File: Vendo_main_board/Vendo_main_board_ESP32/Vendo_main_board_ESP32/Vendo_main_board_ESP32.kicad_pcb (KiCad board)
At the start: 2 copper layers, 60 x 100 mm, 125 parts, among them J1 Screw_Terminal_01x04, J10 Screw_Terminal_01x03, J11 Screw_Terminal_01x02, J12 Screw_Terminal_01x03, J2 Barrel_Jack_MountingPin, J3 Conn_01x05_Pin, J4 Conn_01x05_Pin, J6 Screw_Terminal_01x04, J7 FTDI, J9 Conn_01x04_Pin, Q1 Q_NMOS_Depletion_GSD, Q2 Q_NMOS_Depletion_GSD, Q3 Q_NMOS_Depletion_GSD, Q4 Q_NMOS_Depletion_GSD, SW1 SW_Push, SW2 SW_Push, SW3 SW_Push, SW5 SW_Slide_DPDT, SW7 SW_Push, U1 AMS1117-3.3, U2 TPS54331D, U4 PC817, U5 TPL5010, U6 SOLA-IC SLM1302, U7 ESP32-WROOM-32, Y1 Crystal

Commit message: -esp 32 version done routing
- done routing no unrouted no errors
- warning just silk clipped
- need to take note is the placement of silk such as version control,board name and logo
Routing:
- net GND: track 69.6 -> 81.6 mm, vias 48 -> 147
- net SEG_CLK: track 64.1 -> 65.4 mm
- net RTC_CLK: track 12.8 -> 11.6 mm
- net SEG_DIO: track 67.2 -> 68.0 mm

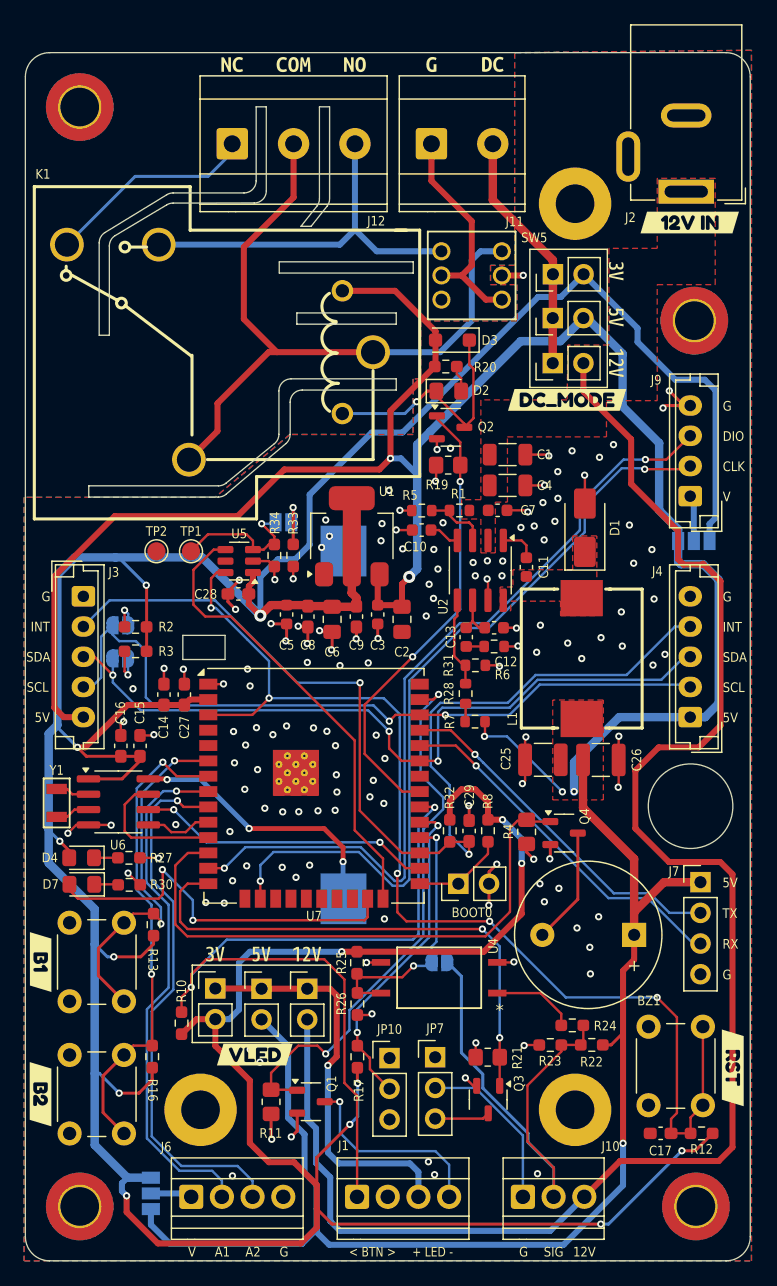
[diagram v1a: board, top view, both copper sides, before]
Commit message: stm32 and esp32 version edit
stm32 ver solid gnd plane to buck conv, adjust buttons to smd , btn1 to 3 and reset
esp32 version adjust slave conn by 1mm far away on the sma hole, adjust button 1 ,2 and reset.
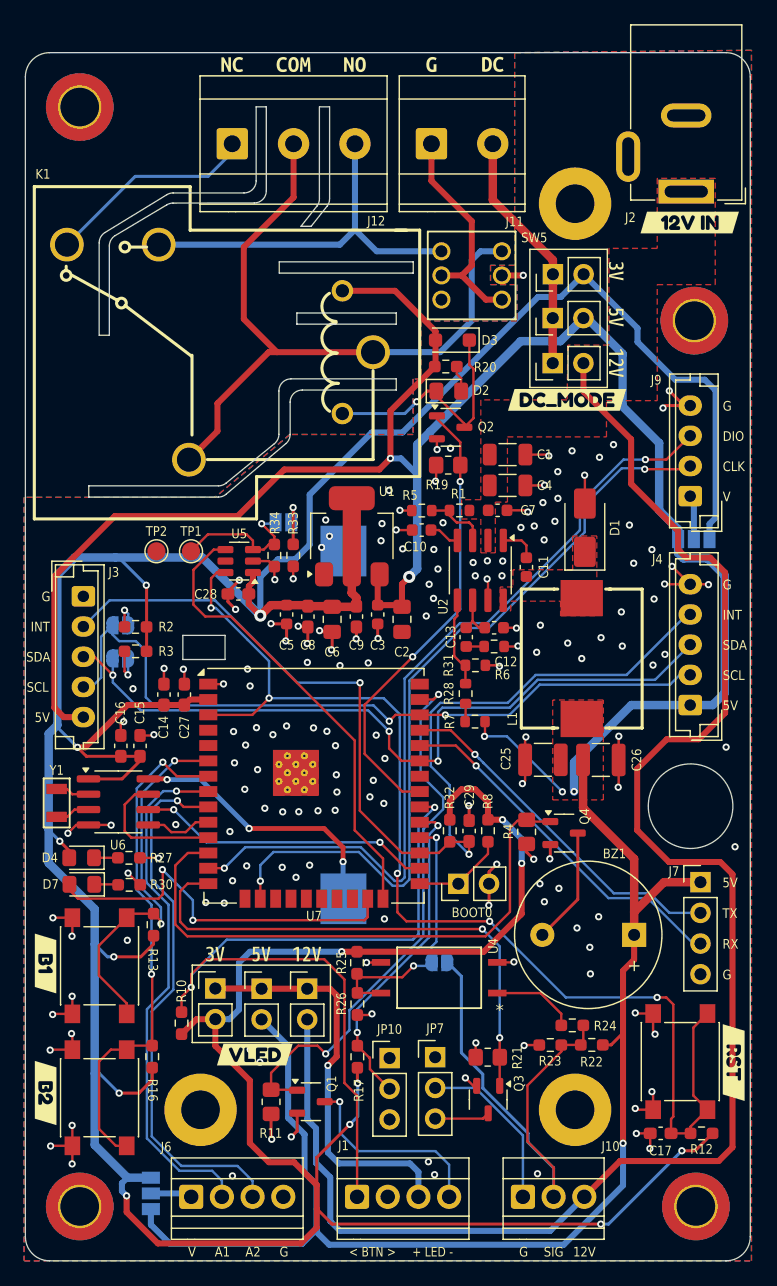
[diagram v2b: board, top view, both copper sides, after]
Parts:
- SW1, SW2, SW3: footprint Button_Switch_THT:SW_PUSH_6mm_H5mm -> Button_Switch_SMD:SW_SPST_PTS645
- moved SW3 3.86 mm to (204.2, 114.1)
- moved SW2 3.85 mm to (204.2, 103.2)
- moved SW1 3.44 mm to (252.3, 111.1)
- moved J4 1.00 mm to (253.1, 81.6)
- moved kibuzzard-6A0C536D 0.45 mm to (256.7, 111.2)
- moved kibuzzard-6A0C57A8 0.43 mm to (199.8, 113.7)
- moved kibuzzard-6A0C57A3 0.42 mm to (199.8, 103.0)
- moved JP6 0.16 mm to (253.4, 67.9)
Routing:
- net GND: track 81.6 -> 110.6 mm, vias 147 -> 168
- net BTN_MODE_2: track 39.7 -> 42.5 mm
- net ESP_EN: track 94.4 -> 96.8 mm
- net BTN_MODE_1: track 30.2 -> 31.4 mm
